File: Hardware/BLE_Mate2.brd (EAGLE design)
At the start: 25.4 x 49.5 mm, 28 parts, among them Q1 BSS138, U2 AP2202-ADJ

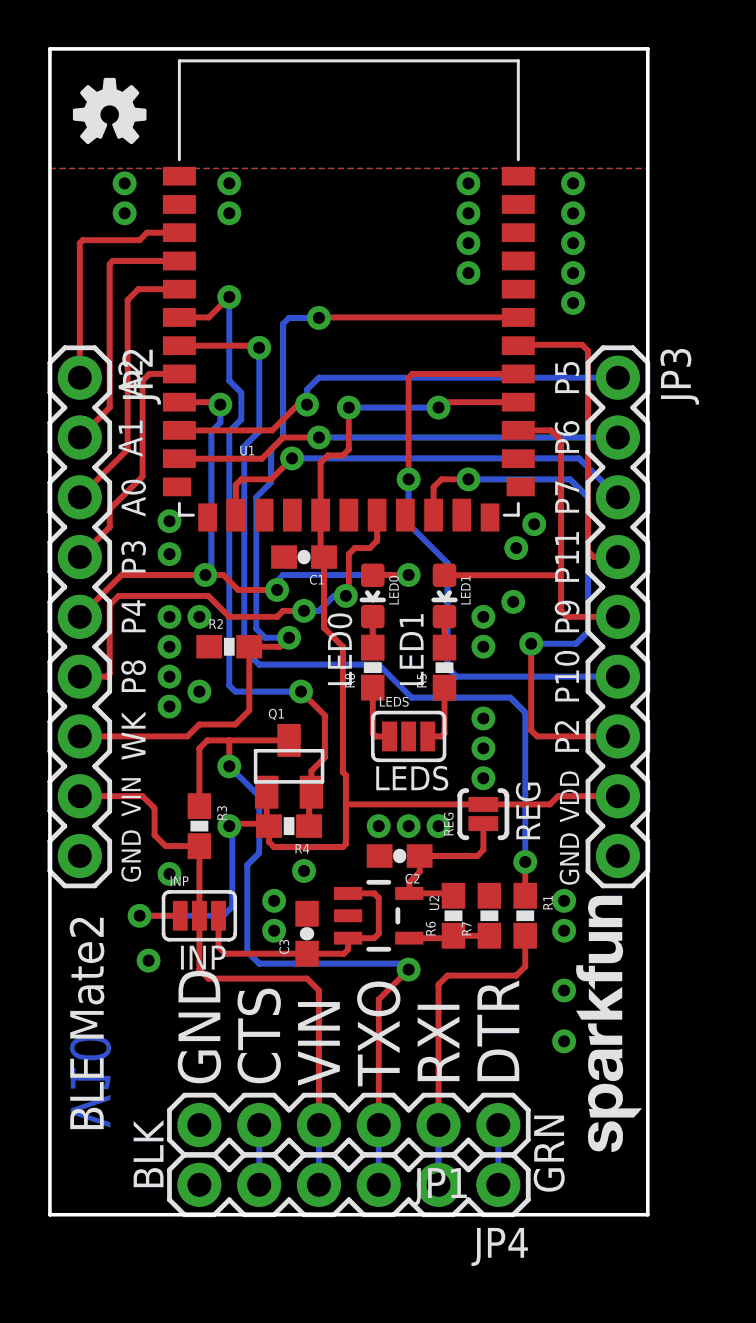
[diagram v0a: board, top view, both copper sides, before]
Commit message: added board fiducials
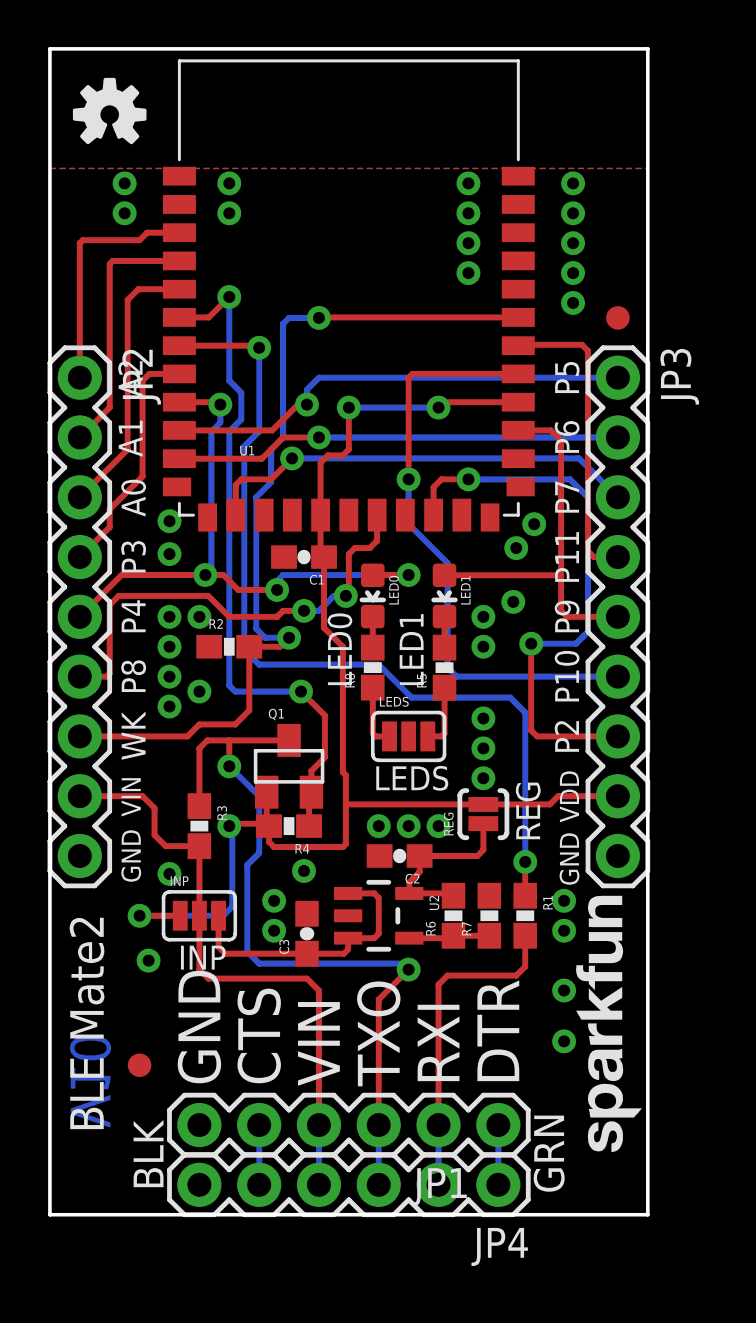
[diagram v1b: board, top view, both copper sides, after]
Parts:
- added FID1, FID2: FIDUCIAL1X2, SparkFun-Aesthetics:FIDUCIAL-1X2
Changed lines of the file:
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@@
 <?xml version="1.0" encoding="utf-8"?>
 <!DOCTYPE eagle SYSTEM "eagle.dtd">
-<eagle version="6.5.0">
+<eagle version="6.6.0">
 <drawing>
 <settings>
@@
 <setting verticaltext="up"/>
 </settings>
-<grid distance="0.05" unitdist="inch" unit="inch" style="lines" multiple="1" display="yes" altdistance="0.005" altunitdist="inch" altunit="inch"/>
+<grid distance="0.05" unitdist="inch" unit="inch" style="lines" multiple="1" display="yes" altdistance="0.01" altunitdist="inch" altunit="inch"/>
 <layers>
 <layer number="1" name="Top" color="4" fill="1" visible="yes" active="yes"/>
-<layer number="2" name="Route2" color="1" fill="3" visible="no" active="yes"/>
-<layer number="15" name="Route15" color="4" fill="6" visible="no" active="yes"/>
+<layer number="2" name="Route2" color="1" fill="3" visible="yes" active="yes"/>
+<layer number="15" name="Route15" color="4" fill="6" visible="yes" active="yes"/>
 <layer number="16" name="Bottom" color="1" fill="1" visible="yes" active="yes"/>
 <layer number="17" name="Pads" color="2" fill="1" visible="yes" active="yes"/>
 <layer number="18" name="Vias" color="2" fill="1" visible="yes" active="yes"/>
 <layer number="19" name="Unrouted" color="6" fill="1" visible="yes" active="yes"/>
-<layer number="20" name="Dimension" color="15" fill="1" visible="yes" active="yes"/>
-<layer number="21" name="tPlace" color="16" fill="1" visible="yes" active="yes"/>
-<layer number="22" name="bPlace" color="14" fill="1" visible="yes" active="yes"/>
+<layer number="20" name="Dimension" color="6" fill="1" visible="yes" active="yes"/>
+<layer number="21" name="tPlace" color="6" fill="1" visible="yes" active="yes"/>
+<layer number="22" name="bPlace" color="6" fill="1" visible="yes" active="yes"/>
 <layer number="23" name="tOrigins" color="15" fill="1" visible="yes" active="yes"/>
 <layer number="24" name="bOrigins" color="15" fill="1" visible="yes" active="yes"/>
-<layer number="25" name="tNames" color="7" fill="1" visible="no" active="yes"/>
-<layer number="26" name="bNames" color="7" fill="1" visible="no" active="yes"/>
-<layer number="27" name="tValues" color="7" fill="1" visible="no" active="yes"/>
-<layer number="28" name="bValues" color="7" fill="1" visible="no" active="yes"/>
-<layer number="29" name="tStop" color="7" fill="3" visible="no" active="yes"/>
-<layer number="30" name="bStop" color="7" fill="6" visible="no" active="yes"/>
-<layer number="31" name="tCream" color="7" fill="4" visible="no" active="yes"/>
-<layer number="32" name="bCream" color="7" fill="5" visible="no" active="yes"/>
-<layer number="39" name="tKeepout" color="4" fill="11" visible="no" active="yes"/>
-<layer number="40" name="bKeepout" color="1" fill="11" visible="no" active="yes"/>
-<layer number="41" name="tRestrict" color="4" fill="10" visible="no" active="yes"/>
-<layer number="42" name="bRestrict" color="1" fill="10" visible="no" active="yes"/>
-<layer number="43" name="vRestrict" color="2" fill="10" visible="no" active="yes"/>
-<layer number="44" name="Drills" color="7" fill="1" visible="no" active="yes"/>
+<layer number="25" name="tNames" color="7" fill="1" visible="yes" active="yes"/>
+<layer number="26" name="bNames" color="7" fill="1" visible="yes" active="yes"/>
+<layer number="27" name="tValues" color="7" fill="1" visible="yes" active="yes"/>
+<layer number="28" name="bValues" color="7" fill="1" visible="yes" active="yes"/>
+<layer number="29" name="tStop" color="7" fill="3" visible="yes" active="yes"/>
+<layer number="30" name="bStop" color="7" fill="6" visible="yes" active="yes"/>
+<layer number="31" name="tCream" color="7" fill="4" visible="yes" active="yes"/>
+<layer number="32" name="bCream" color="7" fill="5" visible="yes" active="yes"/>
+<layer number="39" name="tKeepout" color="4" fill="11" visible="yes" active="yes"/>
+<layer number="40" name="bKeepout" color="1" fill="11" visible="yes" active="yes"/>
+<layer number="41" name="tRestrict" color="4" fill="10" visible="yes" active="yes"/>
+<layer number="42" name="bRestrict" color="1" fill="10" visible="yes" active="yes"/>
+<layer number="43" name="vRestrict" color="2" fill="10" visible="yes" active="yes"/>
+<layer number="44" name="Drills" color="7" fill="1" visible="yes" active="yes"/>
 <layer number="45" name="Holes" color="7" fill="1" visible="yes" active="yes"/>
-<layer number="46" name="Milling" color="3" fill="1" visible="no" active="yes"/>
+<layer number="46" name="Milling" color="3" fill="1" visible="yes" active="yes"/>
 <layer number="51" name="tDocu" color="6" fill="1" visible="yes" active="yes"/>
 <layer number="52" name="bDocu" color="7" fill="1" visible="no" active="no"/>
@@
 <element name="LOGO4" library="SparkFun-Aesthetics" package="OSHW-LOGO-S" value="OSHW-LOGOS" x="-2.159" y="33.02" rot="MR0"/>
 <element name="JP4" library="SparkFun-Connectors" package="1X06" value="" x="13.97" y="-5.08" rot="R180"/>
+<element name="FID1" library="SparkFun-Aesthetics" package="FIDUCIAL-1X2" value="FIDUCIAL1X2" x="-1.27" y="0"/>
+<element name="FID2" library="SparkFun-Aesthetics" package="FIDUCIAL-1X2" value="FIDUCIAL1X2" x="19.05" y="31.75"/>
 </elements>
 <signals>
